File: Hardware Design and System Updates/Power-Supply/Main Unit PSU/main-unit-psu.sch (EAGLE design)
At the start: 11 parts, among them IC1 MCP1703CB, IC2 MCP1703CB

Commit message: Started BOM for main and sub unit psu
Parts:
- B1, G1, IC1, IC2, TR1: OC_NEWARK (none) -> unknown
- C1: MF (none) -> KEMET; MPN (none) -> ESW106M025AC3AA; OC_NEWARK (none) -> 87AC8155
- D1, D3: MF (none) -> ONSEMI; MPN (none) -> 1N4004RLG; OC_NEWARK (none) -> 84K8827
- D2: value (none) -> 1N4004; device diode:ZENER-DIODEDO41Z10 -> diode:1N4004; MF (none) -> ONSEMI; MPN (none) -> 1N4004RLG; OC_NEWARK (none) -> 84K8827
- DC1, DC2: MF (none) -> MURATA POWER SOLUTIONS; MPN (none) -> CME0303S3C; OC_NEWARK (none) -> 29X1501

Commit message: Finished finding parts
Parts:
- TR1: MF (none) -> TRIAD MAGNETICS; MPN (none) -> TCT3-11E07AE; OC_NEWARK unknown -> 98M4353
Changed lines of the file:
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@@
 <part name="X_5" library="ngspice-simulation" library_urn="urn:adsk.eagle:library:527439" deviceset="GND" device=""/>
 <part name="TR1" library="trafo" library_urn="urn:adsk.eagle:library:394" deviceset="EE20-1" device="" package3d_urn="urn:adsk.eagle:package:28342/1">
-<attribute name="MF" value=""/>
-<attribute name="MPN" value=""/>
-<attribute name="OC_NEWARK" value="unknown"/>
+<attribute name="MF" value="TRIAD MAGNETICS"/>
+<attribute name="MPN" value="TCT3-11E07AE"/>
+<attribute name="OC_NEWARK" value="98M4353"/>
 </part>
 <part name="DC1" library="dc-dc-converter" library_urn="urn:adsk.eagle:library:208" deviceset="NME" device="" package3d_urn="urn:adsk.eagle:package:12313/1" value="3.3V">

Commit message: Uploaded main and unit sch
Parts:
- removed G1: CRAA, battery:CRAA
- removed IC2: MCP1703CB, linear:MCP1703CB
- added B2: BK-18650-PC8BK-18650-PC8_MPD, 2023-03-07_13-29-57_Library:BK-18650-PC8BK-18650-PC8_MPD
- added D4, D5: 1N4004, diode:1N4004
- added IC3: V-REG_MCP1700T/MB, 52101-101-REV-A_v16:V-REG_MCP1700T/MB
- added R1: 68 Ohm, rcl:R-US_0204/7
- added R2: 100 Ohm, rcl:R-US_0204/7
- B1: value (none) -> CS10D; OC_NEWARK unknown -> (none)
- C1: MF KEMET -> (none); MPN ESW106M025AC3AA -> (none); OC_NEWARK 87AC8155 -> (none)
- D1, D3: MF ONSEMI -> (none); MPN 1N4004RLG -> (none); OC_NEWARK 84K8827 -> (none)
- D2: value 1N4004 -> NZX9V1B,133; device diode:1N4004 -> diode:ZENER-DIODEDO41Z10; MF ONSEMI -> (none); MPN 1N4004RLG -> (none); OC_NEWARK 84K8827 -> (none)
- DC1, DC2: value 3.3V -> 3.3V DC-DC Converter; MF MURATA POWER SOLUTIONS -> (none); MPN CME0303S3C -> (none); OC_NEWARK 29X1501 -> (none)
- IC1: value MCP1703CB -> V-REG_MCP1700T/MB; device linear:MCP1703CB -> 52101-101-REV-A_v16:V-REG_MCP1700T/MB; OC_NEWARK unknown -> (none)
- TR1: value (none) -> TCT3-11E07AE; MF TRIAD MAGNETICS -> (none); MPN TCT3-11E07AE -> (none); OC_NEWARK 98M4353 -> (none)
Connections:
- new net N$11: D1.A, DC2.+VIN, R1.2, R2.1
- new net N$12: IC1.OUT
- new net N$13: B2.4, B2.6
- new net N$15: D4.C, D5.A
- new net N$16: B2.3, D4.A
- new net N$8: B1.+, C1.1, D2.C, R1.1
- net 0: now also B2.5, R2.2; no longer G1.-
- net N$10: now also IC3.GND; no longer IC2.GND
- net N$3: now also IC3.OUT; no longer B1.+, C1.1, D1.A, D2.C, DC2.+VIN
- net N$4: now also IC1.IN; no longer IC1.VI
- net N$6: now also D5.C; no longer G1.+
- net N$9: now also IC3.IN; no longer IC2.VI
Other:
- moved on the sheet: B1, C1, D3, TR1

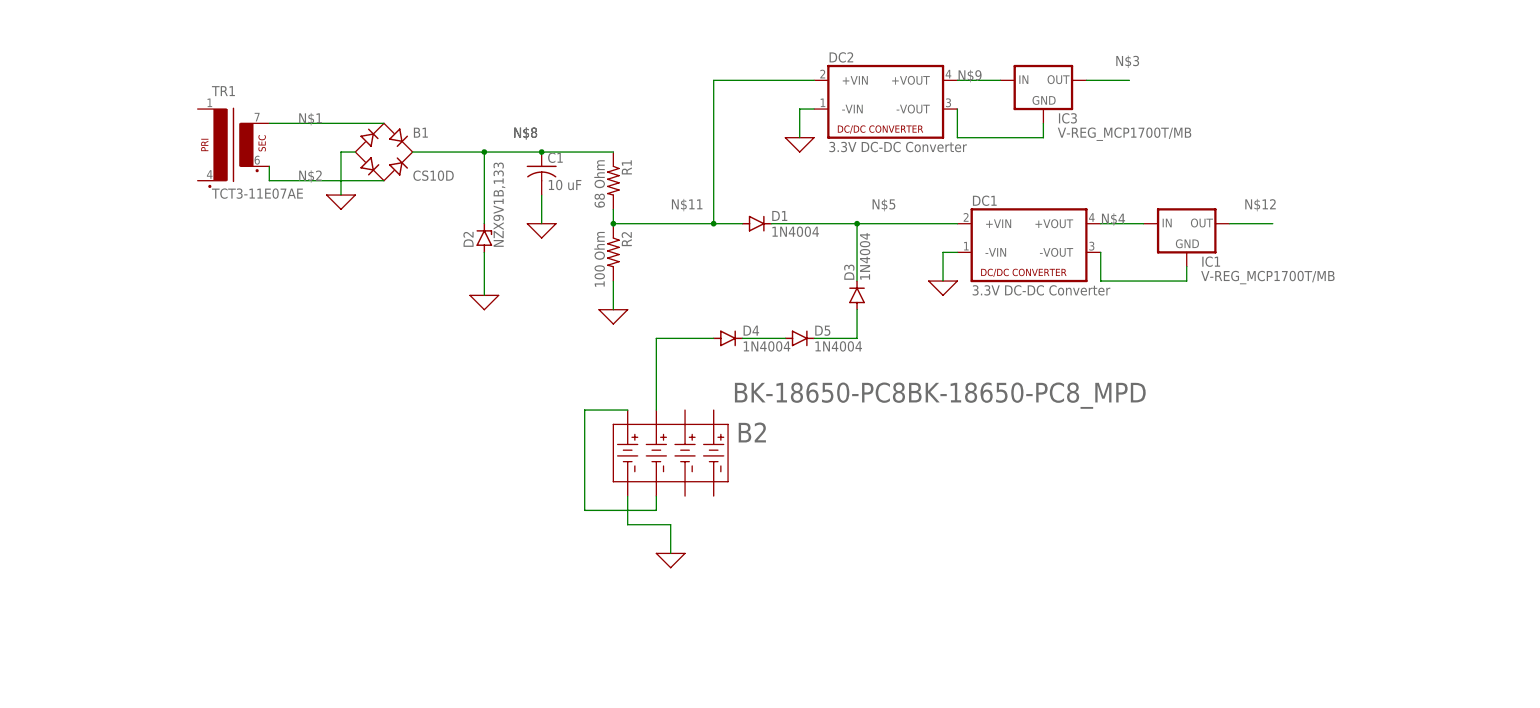
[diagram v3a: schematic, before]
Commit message: Fixed main and sub unit psu sch
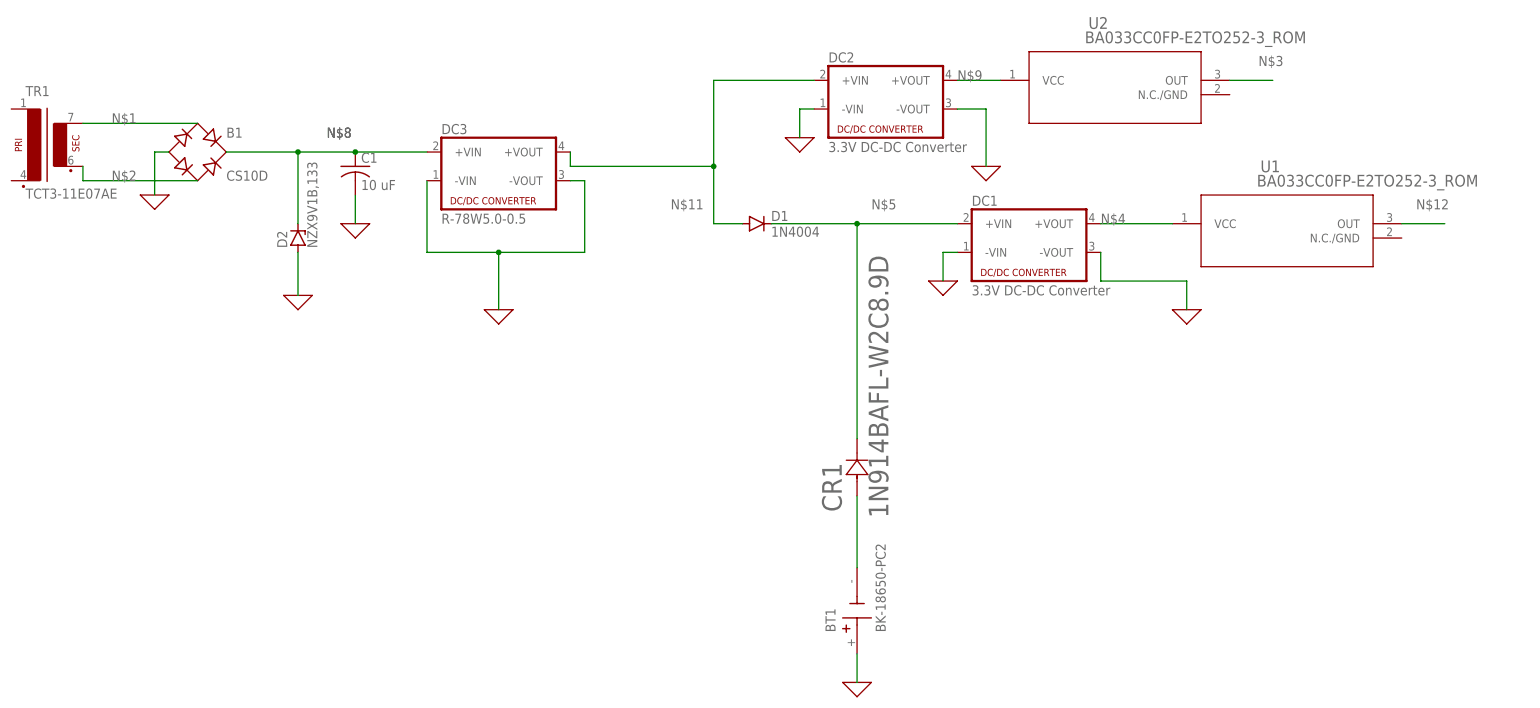
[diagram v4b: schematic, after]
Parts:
- removed B2: BK-18650-PC8BK-18650-PC8_MPD, 2023-03-07_13-29-57_Library:BK-18650-PC8BK-18650-PC8_MPD
- removed D3, D4, D5: 1N4004, diode:1N4004
- removed IC1, IC3: V-REG_MCP1700T/MB, 52101-101-REV-A_v16:V-REG_MCP1700T/MB
- removed R1: 68 Ohm, rcl:R-US_0204/7
- removed R2: 100 Ohm, rcl:R-US_0204/7
- added BT1: BK-18650-PC2, BK-18650-PC2:BK-18650-PC2
- added CR1: 1N914BAFL-W2C8.9D, 2023-03-08_11-41-24_Library:1N914BAFL-W2C8.9D
- added DC3: R-78W5.0-0.5, dc-dc-converter:NME
- added U1, U2: BA033CC0FP-E2TO252-3_ROM, 2023-03-08_12-17-23_Library:BA033CC0FP-E2TO252-3_ROM
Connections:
- removed net N$10: DC2.-VOUT, IC3.GND
- removed net N$13: B2.4, B2.6
- removed net N$15: D4.C, D5.A
- removed net N$16: B2.3, D4.A
- removed net N$7: DC1.-VOUT, IC1.GND
- net 0: now also BT1.+, DC1.-VOUT, DC2.-VOUT, DC3.-VIN, DC3.-VOUT; no longer B2.5, R2.2
- net N$11: now also DC3.+VOUT; no longer R1.2, R2.1
- net N$12: now also U1.OUT; no longer IC1.OUT
- net N$3: now also U2.OUT; no longer IC3.OUT
- net N$4: now also U1.VCC; no longer IC1.IN
- net N$5: now also CR1.1; no longer D3.C
- net N$6: now also BT1.-, CR1.2; no longer D3.A, D5.C
- net N$8: now also DC3.+VIN; no longer R1.1
- net N$9: now also U2.VCC; no longer IC3.IN
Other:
- moved on the sheet: B1, C1, D2, TR1

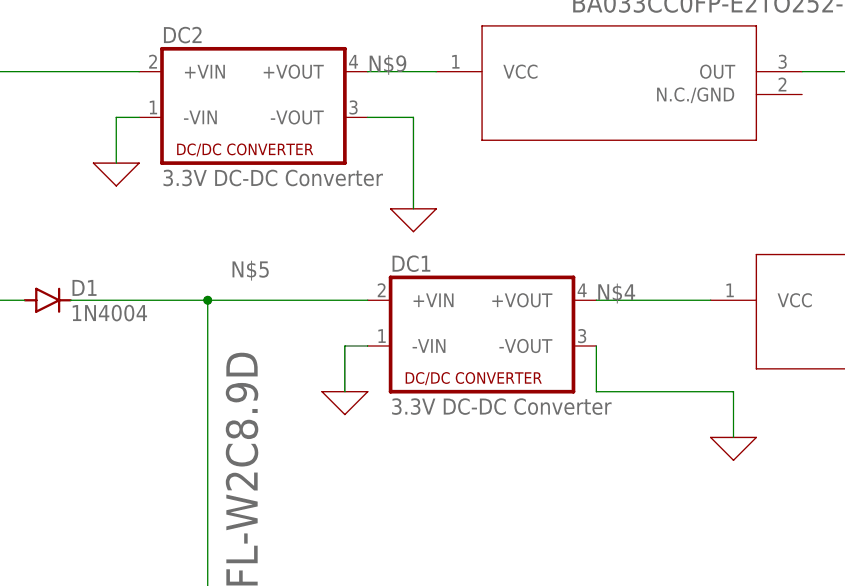
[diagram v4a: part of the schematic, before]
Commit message: Fixed 3.3 regulator and BOM
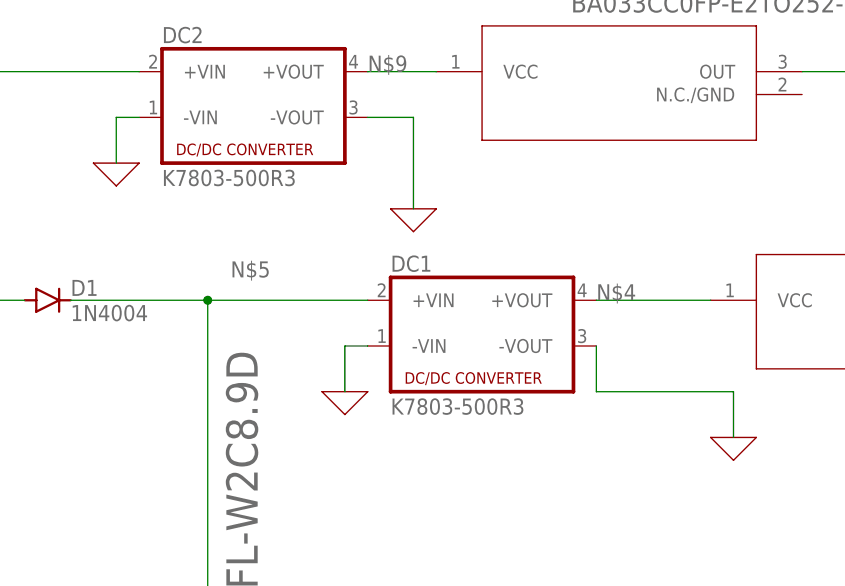
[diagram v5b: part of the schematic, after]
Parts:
- DC1, DC2: value 3.3V DC-DC Converter -> K7803-500R3
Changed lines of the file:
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@@
 <part name="X_3" library="ngspice-simulation" library_urn="urn:adsk.eagle:library:527439" deviceset="GND" device=""/>
 <part name="TR1" library="trafo" library_urn="urn:adsk.eagle:library:394" deviceset="EE20-1" device="" package3d_urn="urn:adsk.eagle:package:28342/1" value="TCT3-11E07AE"/>
-<part name="DC1" library="dc-dc-converter" library_urn="urn:adsk.eagle:library:208" deviceset="NME" device="" package3d_urn="urn:adsk.eagle:package:12313/1" value="3.3V DC-DC Converter"/>
+<part name="DC1" library="dc-dc-converter" library_urn="urn:adsk.eagle:library:208" deviceset="NME" device="" package3d_urn="urn:adsk.eagle:package:12313/1" value="K7803-500R3"/>
 <part name="X_4" library="ngspice-simulation" library_urn="urn:adsk.eagle:library:527439" deviceset="GND" device=""/>
-<part name="DC2" library="dc-dc-converter" library_urn="urn:adsk.eagle:library:208" deviceset="NME" device="" package3d_urn="urn:adsk.eagle:package:12313/1" value="3.3V DC-DC Converter"/>
+<part name="DC2" library="dc-dc-converter" library_urn="urn:adsk.eagle:library:208" deviceset="NME" device="" package3d_urn="urn:adsk.eagle:package:12313/1" value="K7803-500R3"/>
 <part name="X_6" library="ngspice-simulation" library_urn="urn:adsk.eagle:library:527439" deviceset="GND" device=""/>
 <part name="CR1" library="2023-03-08_11-41-24_Library" deviceset="1N914B" device="AFL-W2C8.9D"/>
